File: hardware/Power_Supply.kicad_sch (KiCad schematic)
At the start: 70 parts, among them U18 LTC3122HMSE#PBF, U19 LTC3115IDHD-2#WPBF, U20 NCP1117-3.3_SOT223, U21 NCP1117-12_SOT223, U22 LM2990SX-12

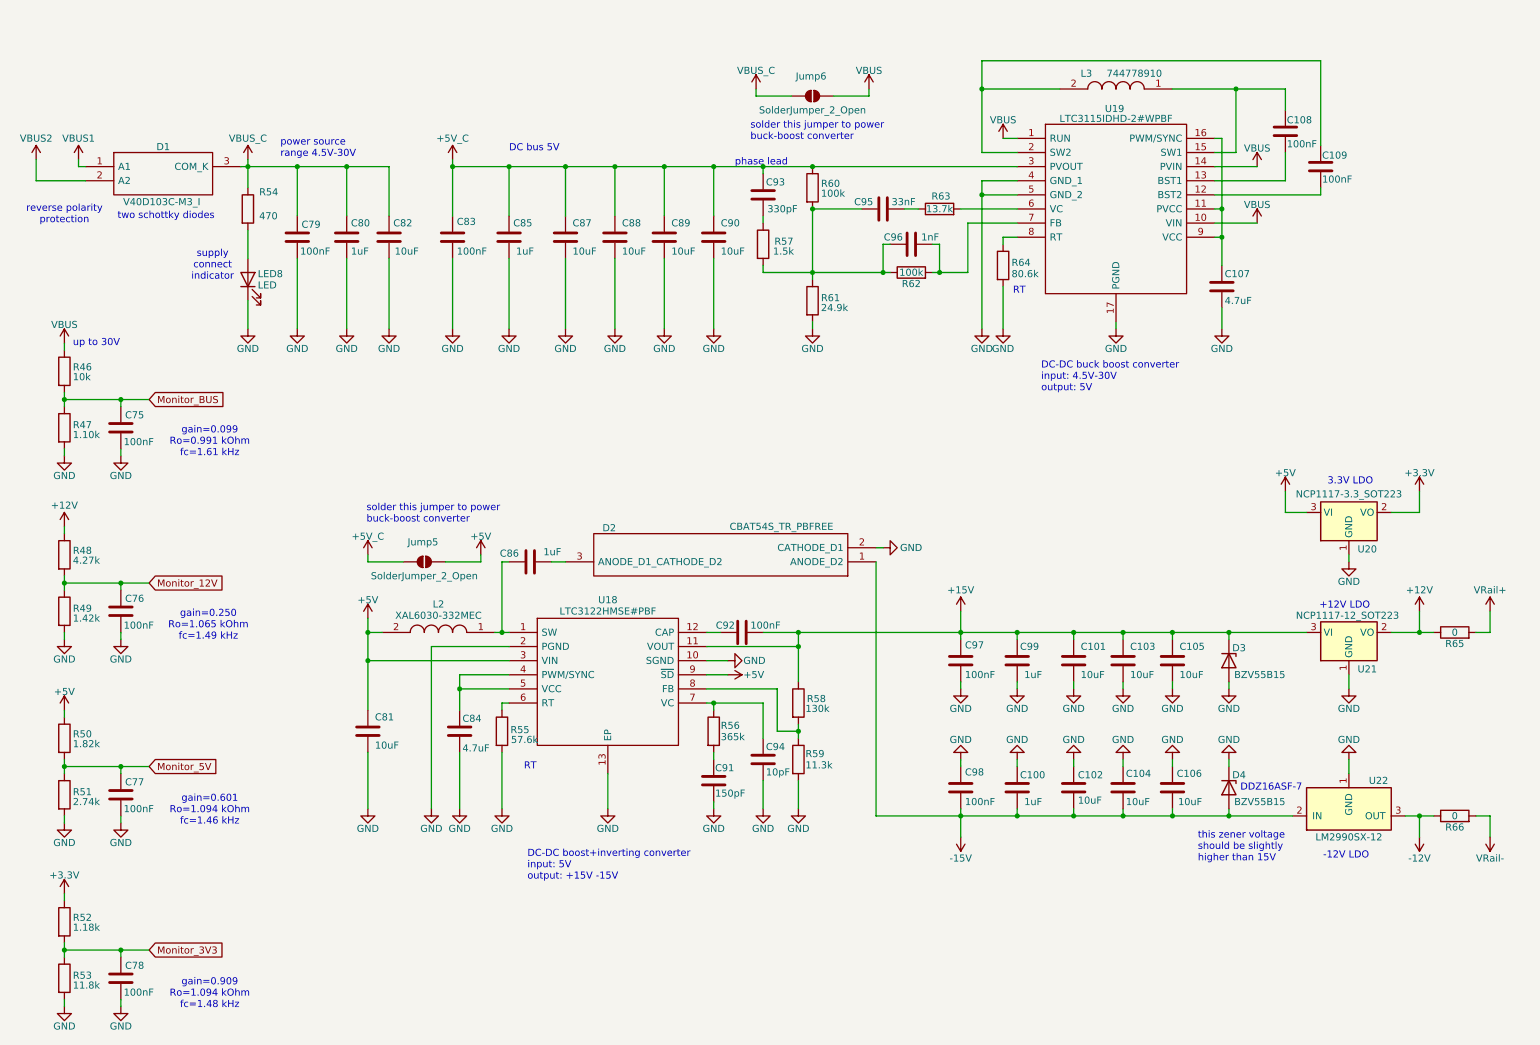
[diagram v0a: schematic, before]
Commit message: Added caps voltage rating + block diagram
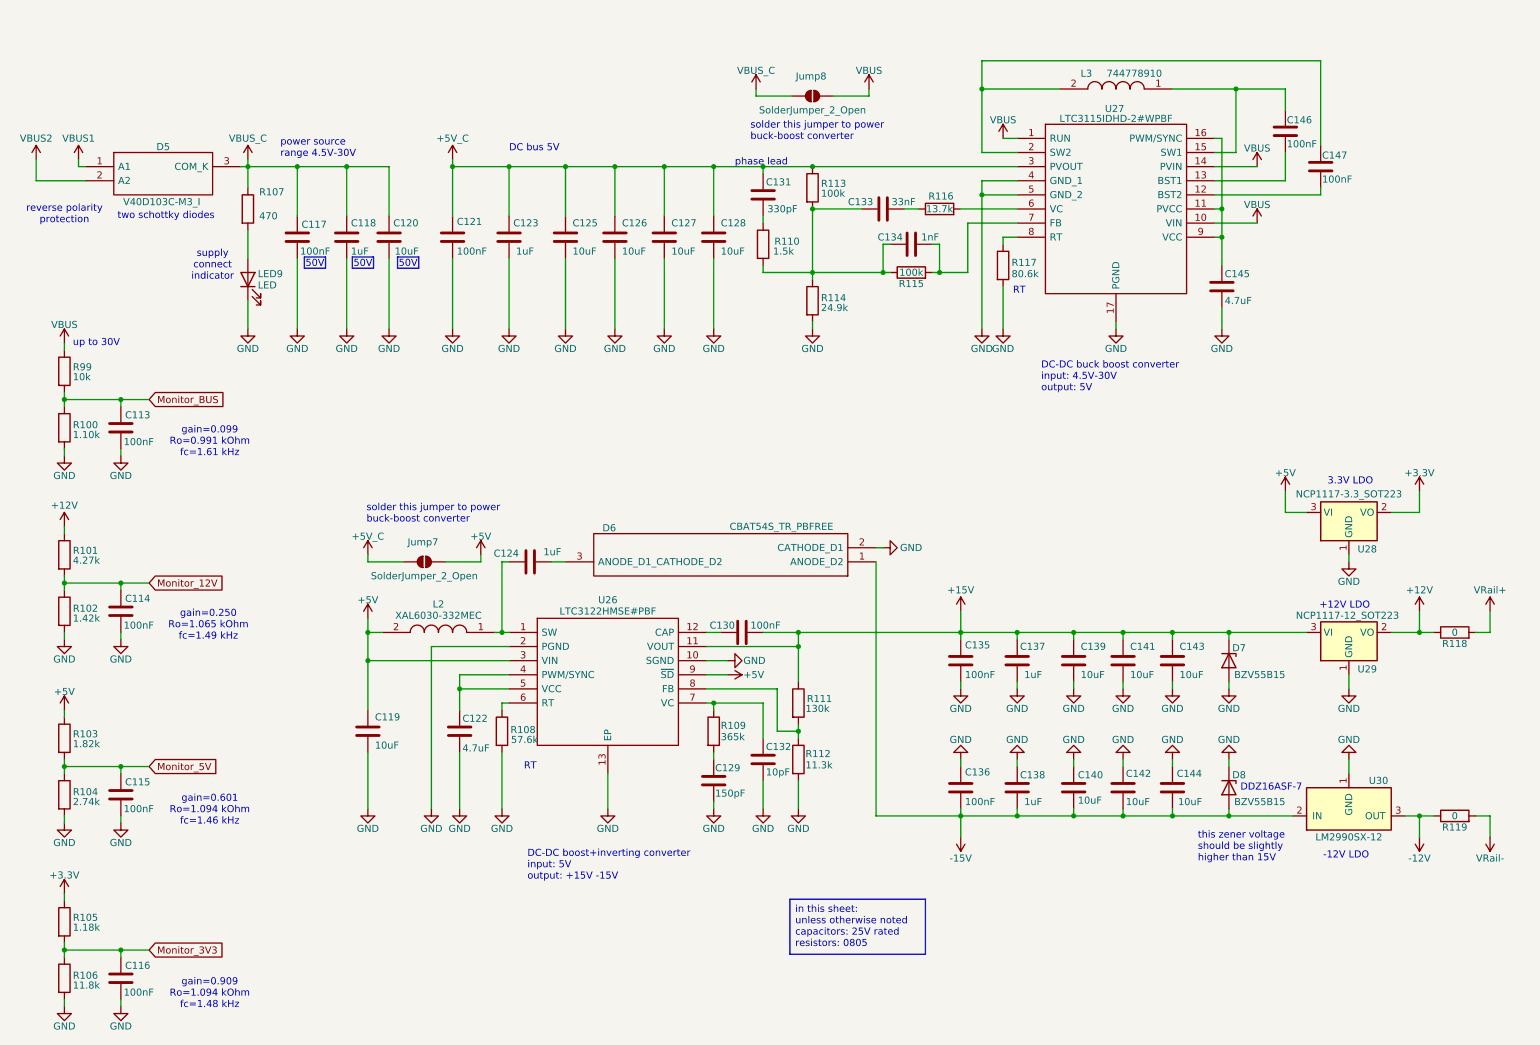
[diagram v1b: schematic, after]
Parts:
- renumbered C75 to C113, C76 to C114, C77 to C115, C78 to C116, C79 to C117, C80 to C118, C81 to C119, C82 to C120, C83 to C121, C84 to C122, C85 to C123, C86 to C124, C87 to C125, C88 to C126, C89 to C127, C90 to C128, C91 to C129, C92 to C130, C93 to C131, C94 to C132, C95 to C133, C96 to C134, C97 to C135, C98 to C136, C99 to C137, C100 to C138, C101 to C139, C102 to C140, C103 to C141, C104 to C142, C105 to C143, C106 to C144, C107 to C145, C108 to C146, C109 to C147, D1 to D5, D2 to D6, D3 to D7, D4 to D8, Jump5 to Jump7, Jump6 to Jump8, LED8 to LED9, R47 to R100, R48 to R101, R49 to R102, R50 to R103, R51 to R104, R52 to R105, R53 to R106, R54 to R107, R55 to R108, R56 to R109, R57 to R110, R58 to R111, R59 to R112, R60 to R113, R61 to R114, R62 to R115, R63 to R116, R64 to R117, R65 to R118, R66 to R119, R46 to R99, U18 to U26, U19 to U27, U20 to U28, U21 to U29, U22 to U30
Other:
- title: Multi Channel HARP DAC -> harp device quad dac

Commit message: The footprint assigning and reviewing have started.
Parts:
- C113, C114, C115, C116, C117, C118, C119, C120, C121, C122, C123, C124, C125, C126, C127, C128, C129, C130, C131, C132, C133, C134, C135, C136, C137, C138, C139, C140, C141, C142, C143, C144, C145, C146, C147: symbol Device:C -> harp.device.quad.dac:C
- D5: symbol V40D103C-M3_I:V40D103C-M3_I -> harp.device.quad.dac:V40D103C-M3_I
- D6: symbol CBAT54S_TR_PBFREE:CBAT54S_TR_PBFREE -> harp.device.quad.dac:CBAT54S_TR_PBFREE
- D7, D8: symbol Diode:BZV55B15 -> harp.device.quad.dac:BZV55B15
- Jump7, Jump8: symbol Jumper:SolderJumper_2_Open -> harp.device.quad.dac:SolderJumper_2_Open
- L2: symbol XAL6030-332MEC:XAL6030-332MEC -> harp.device.quad.dac:XAL6030-332MEC
- L3: symbol 744778910:744778910 -> harp.device.quad.dac:744778910
- LED9: symbol Device:LED -> harp.device.quad.dac:LED
- R100, R101, R102, R103, R104, R105, R106, R107, R108, R109, R110, R111, R112, R113, R114, R115, R116, R117, R118, R119, R99: symbol Device:R -> harp.device.quad.dac:R
- U26: symbol LTC3122HMSE#PBF:LTC3122HMSE#PBF -> harp.device.quad.dac:LTC3122HMSE#PBF
- U27: symbol LTC3115IDHD-2#WPBF:LTC3115IDHD-2#WPBF -> harp.device.quad.dac:LTC3115IDHD-2#WPBF
- U28: symbol Regulator_Linear:NCP1117-3.3_SOT223 -> harp.device.quad.dac:NCP1117-3.3_SOT223
- U29: symbol Regulator_Linear:NCP1117-12_SOT223 -> harp.device.quad.dac:NCP1117-12_SOT223
- U30: symbol Regulator_Linear:LM2990SX-12 -> harp.device.quad.dac:LM2990SX-12

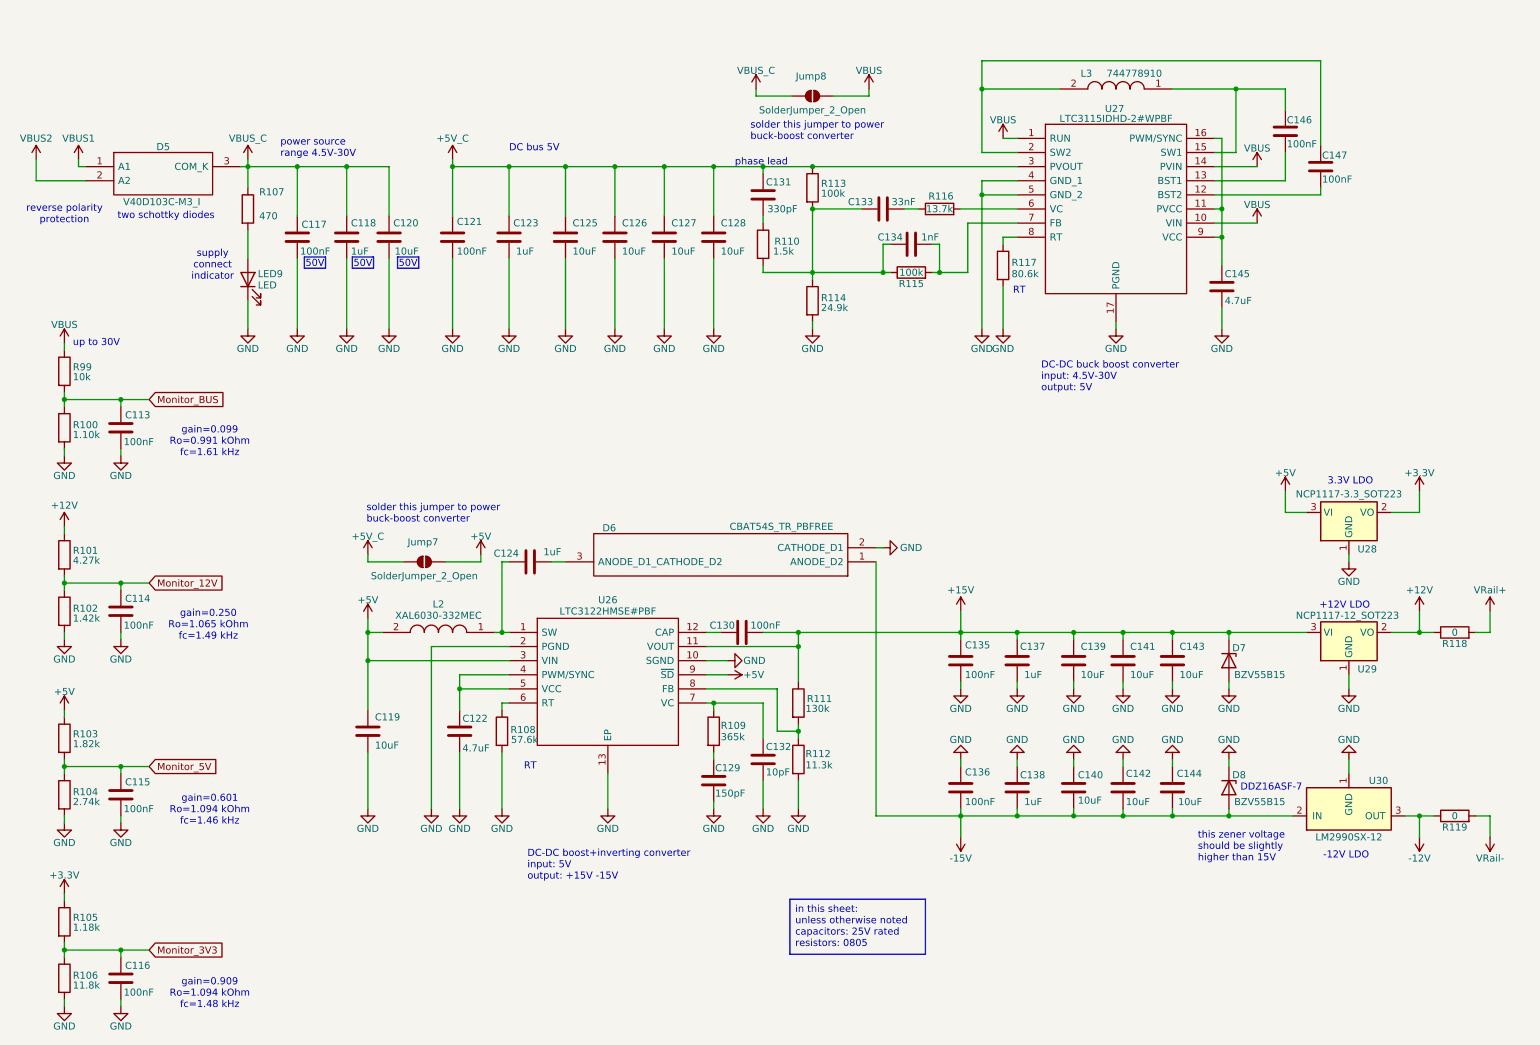
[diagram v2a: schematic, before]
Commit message: Modified notes about caps and resistors
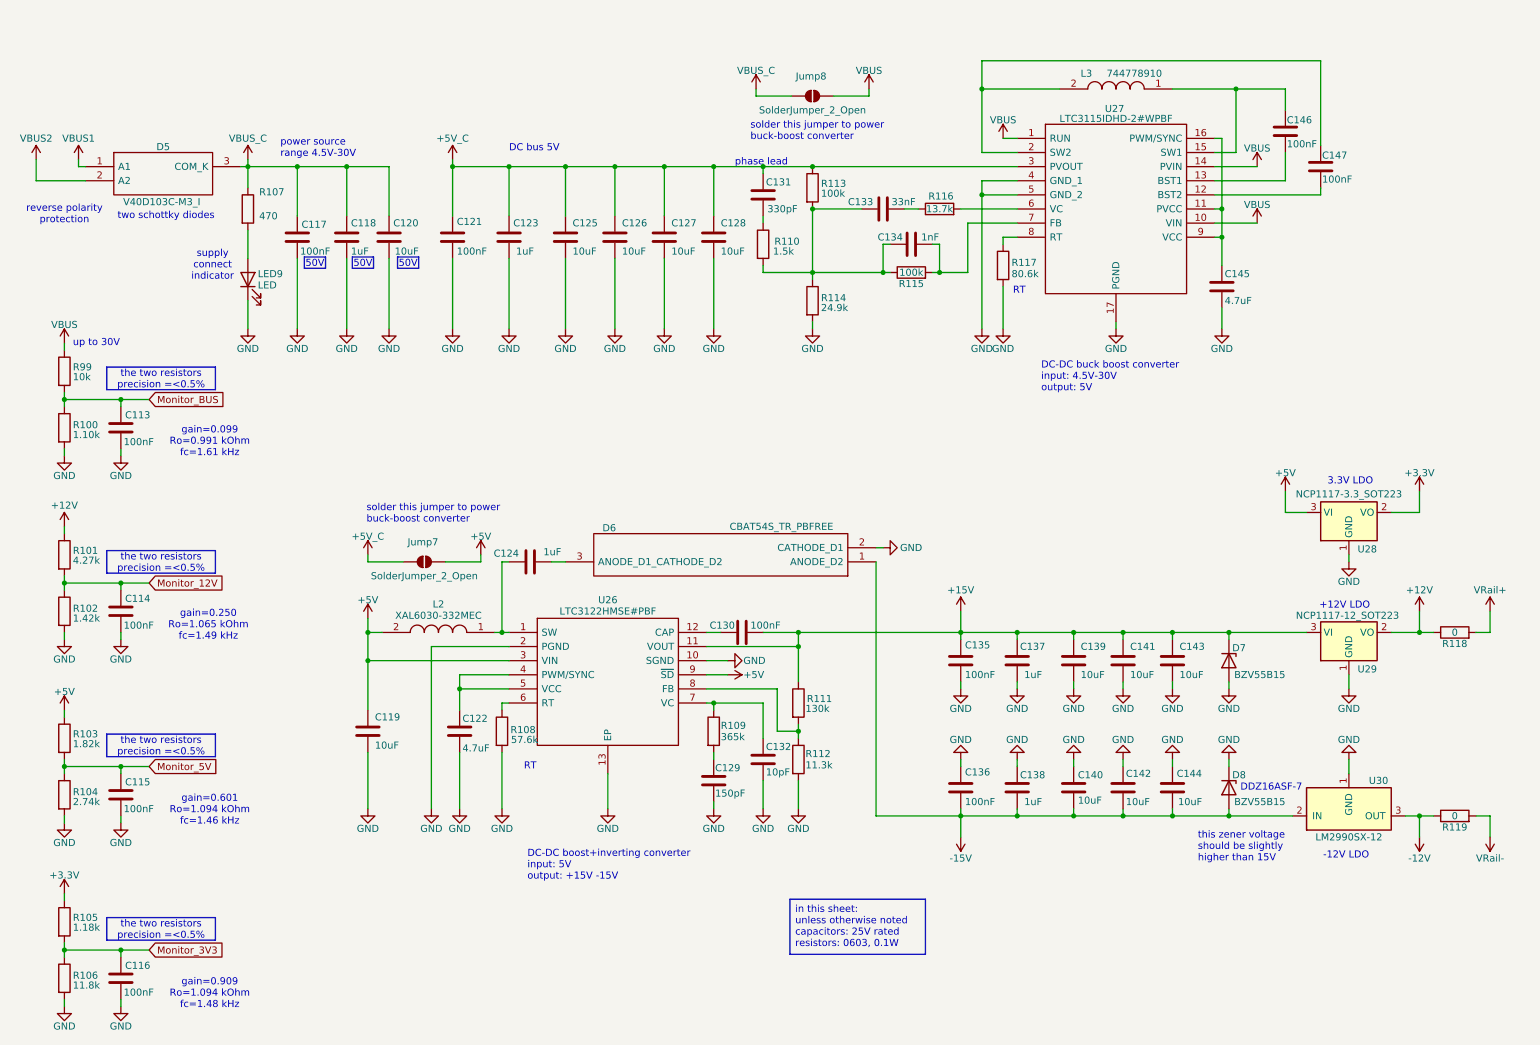
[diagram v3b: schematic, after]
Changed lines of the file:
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@@
 		)
 	)
-	(text_box "in this sheet:\nunless otherwise noted\ncapacitors: 25V rated \nresistors: 0805"
+	(text_box "in this sheet:\nunless otherwise noted\ncapacitors: 25V rated \nresistors: 0603, 0.1W"
 		(exclude_from_sim no)
 		(at 152.146 166.116 0)
@@
 		)
 	)
+	(text_box "the two resistors\nprecision =<0.5%"
+		(exclude_from_sim no)
+		(at 29.21 136.398 0)
+		(size 19.558 4.064)
+		(margins 0.9525 0.9525 0.9525 0.9525)
+		(stroke
+			(width 0)
+			(type solid)
+		)
+		(fill
+			(type color)
+			(color 0 255 0 1)
+		)
+		(effects
+			(font
+				(size 1.27 1.27)
+			)
+		)
+	)
+	(text_box "the two resistors\nprecision =<0.5%"
+		(exclude_from_sim no)
+		(at 29.21 169.418 0)
+		(size 19.558 4.064)
+		(margins 0.9525 0.9525 0.9525 0.9525)
+		(stroke
+			(width 0)
+			(type solid)
+		)
+		(fill
+			(type color)
+			(color 0 255 0 1)
+		)
+		(effects
+			(font
+				(size 1.27 1.27)
+			)
+		)
+	)
 	(text_box "50V"
 		(exclude_from_sim no)
@@
 		(margins 0.9525 0.9525 0.9525 0.9525)
 		(stroke
+			(width 0)
+			(type solid)
+		)
+		(fill
+			(type color)
+			(color 0 255 0 1)
+		)
+		(effects
+			(font
+				(size 1.27 1.27)
+			)
+		)
+	)
+	(text_box "the two resistors\nprecision =<0.5%"
+		(exclude_from_sim no)
+		(at 29.21 103.378 0)
+		(size 19.558 4.064)
+		(margins 0.9525 0.9525 0.9525 0.9525)
+		(stroke
+			(width 0)
+			(type solid)
+		)
+		(fill
+			(type color)
+			(color 0 255 0 1)
+		)
+		(effects
+			(font
+				(size 1.27 1.27)
+			)
+		)
+	)
+	(text_box "the two resistors\nprecision =<0.5%"
+		(exclude_from_sim no)
+		(at 29.21 70.358 0)
+		(size 19.558 4.064)
+		(margins 0.9525 0.9525 0.9525 0.9525)
+		(stroke

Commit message: Updating some footprints
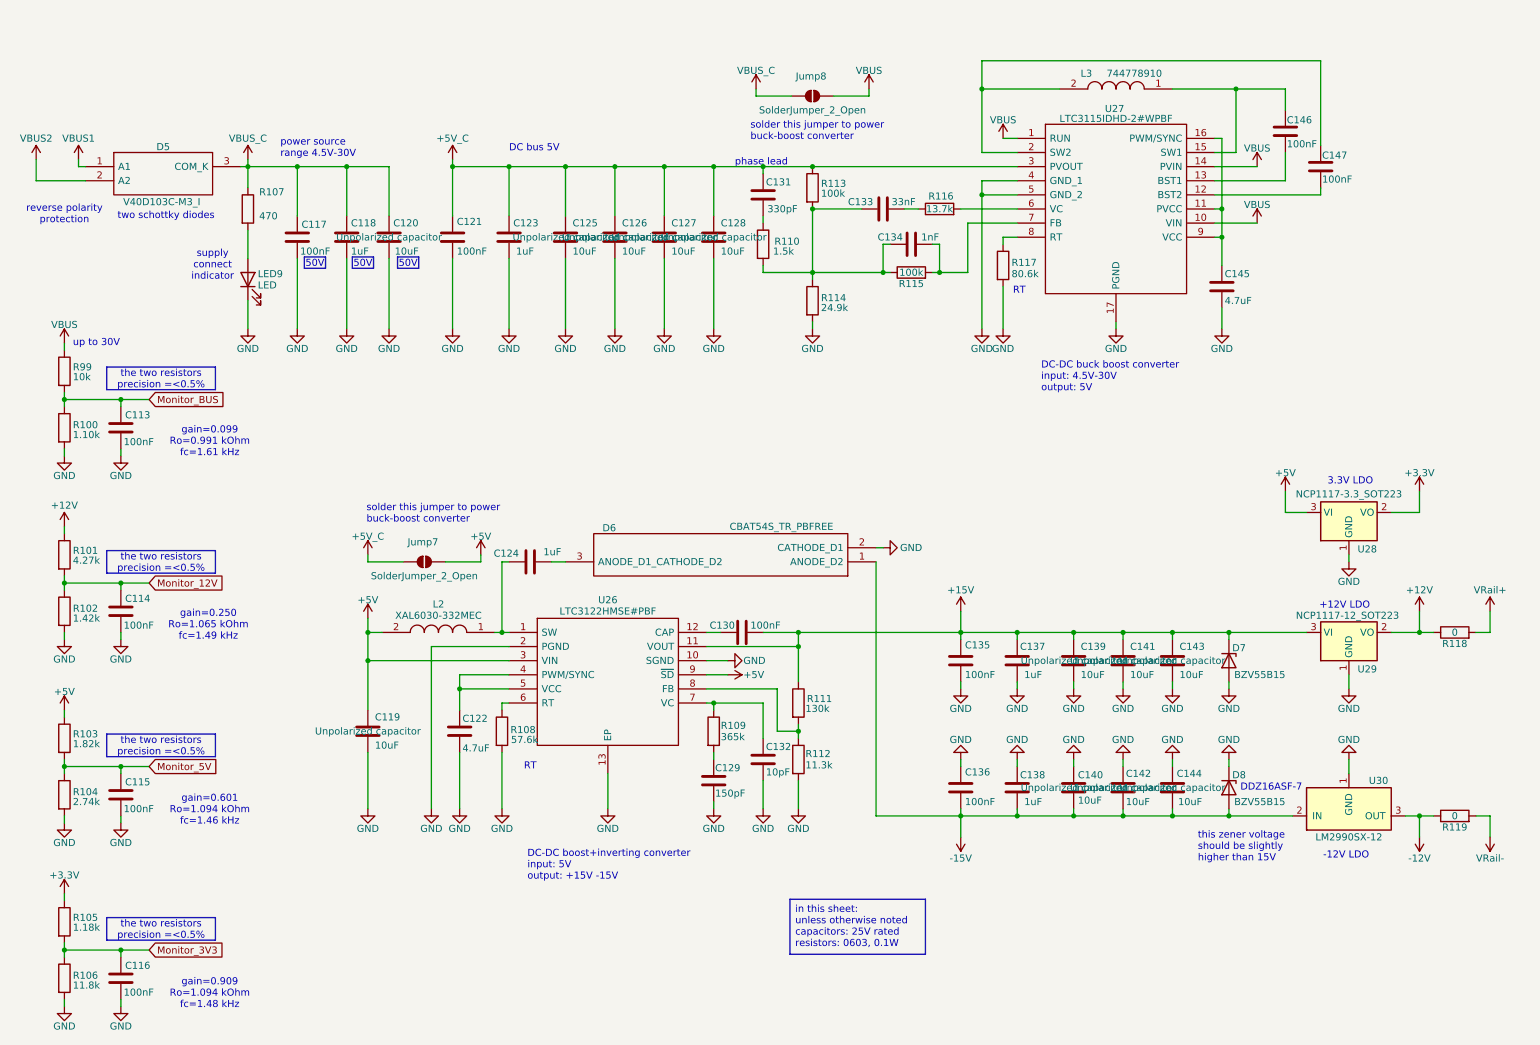
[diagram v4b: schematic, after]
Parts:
- C113, C114, C115, C116, C117, C118, C121, C123, C124, C129, C130, C131, C132, C133, C134, C135, C136, C137, C138, C146, C147: footprint Capacitor_SMD:C_0402_1005Metric -> Capacitor_SMD:C_0603_1608Metric; symbol harp.device.quad.dac:C -> harp.device.quad.dac:C_0603
- C119, C122, C125, C126, C127, C128, C139, C140, C141, C142, C143, C144, C145: footprint Capacitor_SMD:C_0805_2012Metric -> Capacitor_SMD:C_0603_1608Metric; symbol harp.device.quad.dac:C -> harp.device.quad.dac:C_0603
- C120: footprint Capacitor_SMD:C_0805_2012Metric -> Capacitor_SMD:C_1206_3216Metric; symbol harp.device.quad.dac:C -> harp.device.quad.dac:C_1206
- D6: footprint KiCad:SOT95P230X109-3N -> SOT95P230X109-3N
- Jump7, Jump8: footprint (none) -> harp.device.quad.dac.kicad:R_0603_1608Metric_Pad0.98x0.95mm_HandSolder
- LED9: footprint LED_SMD:LED_0603_1608Metric_Pad1.05x0.95mm_HandSolder -> harp.device.quad.dac.kicad:LED_0603_1608Metric_Pad1.05x0.95mm_HandSolder; MFN (none) -> SunLED; MPN (none) -> XZCDGK53W-1VF
- R100, R101, R102, R103, R104, R105, R106, R107, R108, R109, R110, R111, R112, R113, R114, R115, R116, R117, R118, R119, R99: footprint Resistor_SMD:R_0402_1005Metric -> Resistor_SMD:R_0603_1608Metric; symbol harp.device.quad.dac:R -> harp.device.quad.dac:R_0603

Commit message: The layout design has begun.
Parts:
- added J25, J26: Conn_01x02, Connector_PinHeader_2.54mm:PinHeader_1x02_P2.54mm_Vertical, symbol harp.device.quad.dac:Conn_01x02
- D5: footprint V40D103CM3I -> harp.device.quad.dac.kicad:V40D103CM3I
- D6: footprint SOT95P230X109-3N -> harp.device.quad.dac.kicad:SOT95P230X109-3N
- D7, D8: footprint Diode_SMD:D_MiniMELF -> harp.device.quad.dac.kicad:D_MiniMELF
- L2: footprint XAL6030182MEB -> harp.device.quad.dac.kicad:XAL6030182MEB
- L3: footprint WE-PD_7332/7345_PLASTIC_BASE54 -> harp.device.quad.dac.kicad:WE-PD_7332-7345_PLASTIC_BASE54
- U26: footprint SOP65P490X110-13N -> harp.device.quad.dac.kicad:SOP65P490X110-13N
- U27: footprint SON50P400X500X80-17N-D -> harp.device.quad.dac.kicad:SON50P400X500X80-17N-D
- U28, U29: footprint Package_TO_SOT_SMD:SOT-223-3_TabPin2 -> harp.device.quad.dac.kicad:SOT-223-3_TabPin2
- U30: footprint (none) -> harp.device.quad.dac.kicad:KTT0003B
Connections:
- net +5V: now also J25.2 (Pin_2)
- net +5V_C: now also J25.1 (Pin_1)
- net -15V: now also U30.4 (IN), U30.5 (IN), U30.6 (IN)
- net VBUS: now also J26.2 (Pin_2)
- net VBUS_C: now also J26.1 (Pin_1)
